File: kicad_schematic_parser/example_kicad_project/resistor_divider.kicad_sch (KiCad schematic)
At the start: 3 parts

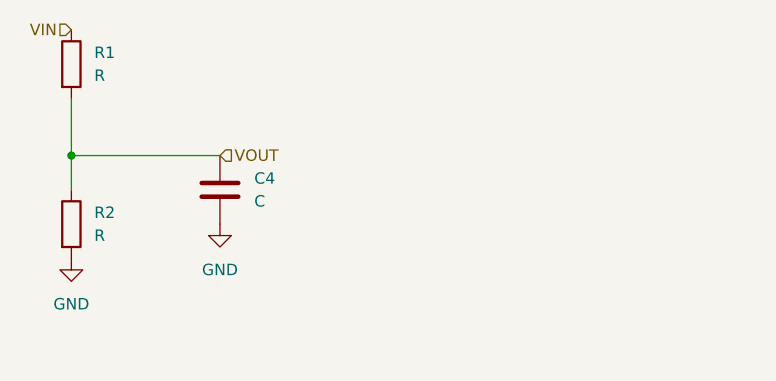
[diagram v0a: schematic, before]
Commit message: add formatting
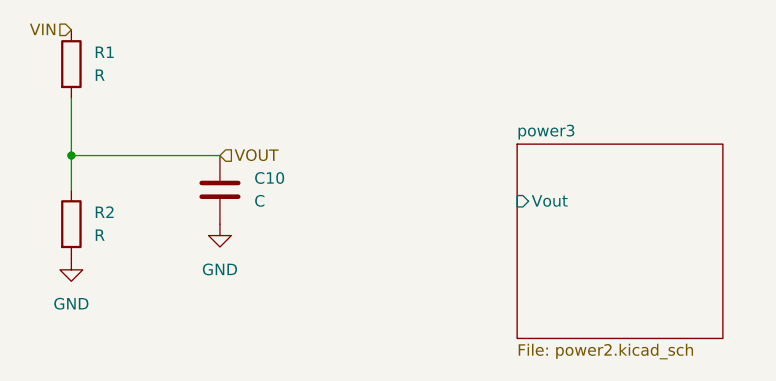
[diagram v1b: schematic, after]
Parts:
- renumbered C4 to C10
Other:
- added sheet power3 (power2.kicad_sch)
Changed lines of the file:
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@@
 		(dnp no)
 		(fields_autoplaced yes)
-		(property "Reference" "#PWR04"
+		(property "Reference" "#PWR025"
 			(at 121.92 91.44 0)
 			(effects
@@
 		)
 		(instances
-			(project ""
-				(path "/139408cf-b4ac-4ccf-8751-afbb6def1f13/7dcd522d-d03d-41f6-bad3-56f1f937b049"
-					(reference "#PWR04")
+			(project "example_kicad_project"
+				(path "/139408cf-b4ac-4ccf-8751-afbb6def1f13/e6f5f316-cb92-4d26-9a5c-0bb6c841d4b0/0f8673e0-e78a-49db-bb03-1ef92ea13213"
+					(reference "#PWR025")
 					(unit 1)
 				)
@@
 					(unit 1)
 				)
+				(path "/139408cf-b4ac-4ccf-8751-afbb6def1f13/e6f5f316-cb92-4d26-9a5c-0bb6c841d4b0/0f8673e0-e78a-49db-bb03-1ef92ea13213"
+					(reference "#PWR028")
+					(unit 1)
+				)
 			)
 		)
@@
 					(unit 1)
 				)
+				(path "/139408cf-b4ac-4ccf-8751-afbb6def1f13/e6f5f316-cb92-4d26-9a5c-0bb6c841d4b0/0f8673e0-e78a-49db-bb03-1ef92ea13213"
+					(reference "R10")
+					(unit 1)
+				)
 			)
 		)
@@
 					(unit 1)
 				)
+				(path "/139408cf-b4ac-4ccf-8751-afbb6def1f13/e6f5f316-cb92-4d26-9a5c-0bb6c841d4b0/0f8673e0-e78a-49db-bb03-1ef92ea13213"
+					(reference "R9")
+					(unit 1)
+				)
 			)
 		)
@@
 		(dnp no)
 		(fields_autoplaced yes)
-		(property "Reference" "C4"
+		(property "Reference" "C10"
 			(at 142.24 76.1999 0)
 			(effects
@@
 		)
 		(instances
-			(project ""
+			(project "example_kicad_project"
+				(path "/139408cf-b4ac-4ccf-8751-afbb6def1f13/e6f5f316-cb92-4d26-9a5c-0bb6c841d4b0/0f8673e0-e78a-49db-bb03-1ef92ea13213"
+					(reference "C10")
+					(unit 1)
+				)
+			)
+		)
+	)
+	(sheet
+		(at 171.45 72.39)
+		(size 22.86 21.59)
+		(fields_autoplaced yes)
+		(stroke
+			(width 0.1524)
+			(type solid)
+		)
+		(fill
+			(color 0 0 0 0.0000)
+		)
+		(property "Sheetname" "power3"
+			(at 171.45 71.6784 0)
+			(effects
+				(font
+					(size 1.27 1.27)
+				)
+				(justify left bottom)
+			)
+		)
+		(property "Sheetfile" "power2.kicad_sch"
+			(at 171.45 94.5646 0)
+			(effects
+				(font
+					(size 1.27 1.27)
+				)
+				(justify left top)
+			)
+		)
+		(pin "Vout" input
+			(at 171.45 78.74 180)
+			(effects
+				(font
+					(size 1.27 1.27)
+				)
+				(justify left)
+			)
+		)
+		(instances
+			(project "example_kicad_project"
 				(path "/139408cf-b4ac-4ccf-8751-afbb6def1f13/7dcd522d-d03d-41f6-bad3-56f1f937b049"
-					(reference "C4")
-					(unit 1)
-				)
-			)
+					(page "8")
+				)
+				(path "/139408cf-b4ac-4ccf-8751-afbb6def1f13/e6f5f316-cb92-4d26-9a5c-0bb6c841d4b0/0f8673e0-e78a-49db-bb03-1ef92ea13213"
+					(page "9")
+				)
+			)

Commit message: change to esp32 project, make more practical
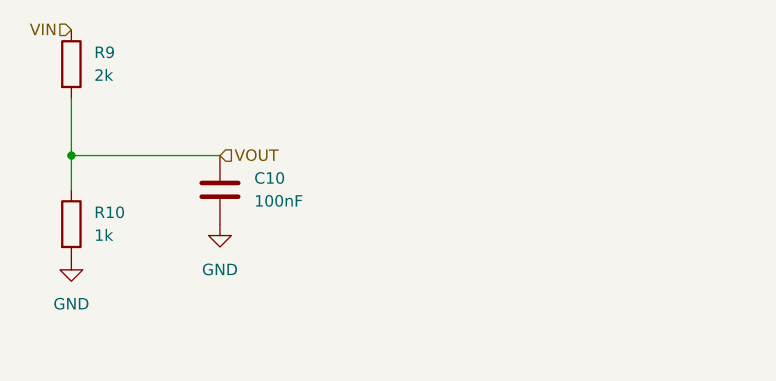
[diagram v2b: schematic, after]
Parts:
- C10: value C -> 100nF
- R10: renamed from R2; value R -> 1k
- R9: renamed from R1; value R -> 2k
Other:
- removed sheet power3
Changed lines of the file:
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@@
 		(dnp no)
 		(fields_autoplaced yes)
-		(property "Reference" "#PWR07"
+		(property "Reference" "#PWR028"
 			(at 138.43 87.63 0)
 			(effects
@@
 		(instances
 			(project "example_kicad_project"
-				(path "/139408cf-b4ac-4ccf-8751-afbb6def1f13/7dcd522d-d03d-41f6-bad3-56f1f937b049"
-					(reference "#PWR07")
-					(unit 1)
-				)
 				(path "/139408cf-b4ac-4ccf-8751-afbb6def1f13/e6f5f316-cb92-4d26-9a5c-0bb6c841d4b0/0f8673e0-e78a-49db-bb03-1ef92ea13213"
 					(reference "#PWR028")
@@
 		(dnp no)
 		(fields_autoplaced yes)
-		(property "Reference" "R2"
+		(property "Reference" "R10"
 			(at 124.46 80.0099 0)
 			(effects
@@
 			)
 		)
-		(property "Value" "R"
+		(property "Value" "1k"
 			(at 124.46 82.5499 0)
 			(effects
@@
 		(instances
 			(project "example_kicad_project"
-				(path "/139408cf-b4ac-4ccf-8751-afbb6def1f13/7dcd522d-d03d-41f6-bad3-56f1f937b049"
-					(reference "R2")
-					(unit 1)
-				)
 				(path "/139408cf-b4ac-4ccf-8751-afbb6def1f13/e6f5f316-cb92-4d26-9a5c-0bb6c841d4b0/0f8673e0-e78a-49db-bb03-1ef92ea13213"
 					(reference "R10")
@@
 		(dnp no)
 		(fields_autoplaced yes)
-		(property "Reference" "R1"
+		(property "Reference" "R9"
 			(at 124.46 62.2299 0)
 			(effects
@@
 			)
 		)
-		(property "Value" "R"
+		(property "Value" "2k"
 			(at 124.46 64.7699 0)
 			(effects
@@
 		(instances
 			(project "example_kicad_project"
-				(path "/139408cf-b4ac-4ccf-8751-afbb6def1f13/7dcd522d-d03d-41f6-bad3-56f1f937b049"
-					(reference "R1")
-					(unit 1)
-				)
 				(path "/139408cf-b4ac-4ccf-8751-afbb6def1f13/e6f5f316-cb92-4d26-9a5c-0bb6c841d4b0/0f8673e0-e78a-49db-bb03-1ef92ea13213"
 					(reference "R9")
@@
 			)
 		)
-		(property "Value" "C"
+		(property "Value" "100nF"
 			(at 142.24 78.7399 0)
 			(effects
@@
 				)
 			)
-		)
-	)
-	(sheet
-		(at 171.45 72.39)
-		(size 22.86 21.59)
-		(fields_autoplaced yes)
-		(stroke
-			(width 0.1524)
-			(type solid)
-		)
-		(fill
-			(color 0 0 0 0.0000)
-		)
-		(property "Sheetname" "power3"
-			(at 171.45 71.6784 0)
-			(effects
-				(font
-					(size 1.27 1.27)
-				)
-				(justify left bottom)
-			)
-		)
-		(property "Sheetfile" "power2.kicad_sch"
-			(at 171.45 94.5646 0)
-			(effects
-				(font
-					(size 1.27 1.27)
-				)
-				(justify left top)
-			)
-		)
-		(pin "Vout" input
-			(at 171.45 78.74 180)
-			(effects
-				(font
-					(size 1.27 1.27)
-				)
-				(justify left)
-			)
-		)
-		(instances
-			(project "example_kicad_project"
-				(path "/139408cf-b4ac-4ccf-8751-afbb6def1f13/7dcd522d-d03d-41f6-bad3-56f1f937b049"
-					(page "8")
-				)
-				(path "/139408cf-b4ac-4ccf-8751-afbb6def1f13/e6f5f316-cb92-4d26-9a5c-0bb6c841d4b0/0f8673e0-e78a-49db-bb03-1ef92ea13213"
-					(page "9")
-				)
-			)
